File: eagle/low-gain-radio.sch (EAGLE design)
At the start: 124 parts, among them U1 MKW01Z128, U2 SKY65116, U3 W25Q80DV, U4 LP5907MFX-3.3, U5 NC7SZ05, U6 LP5907MFX-3.3, U7 LD39200, U8 MAAL-010704, U9 SKY13405-490LF, Y1 32MHz

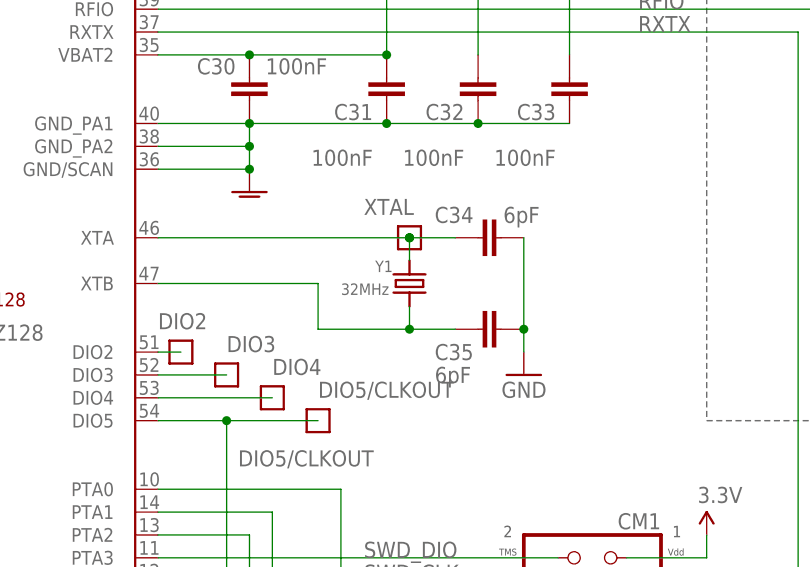
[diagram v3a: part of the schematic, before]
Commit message: Changed crystal symbol to get gnd working on the layout
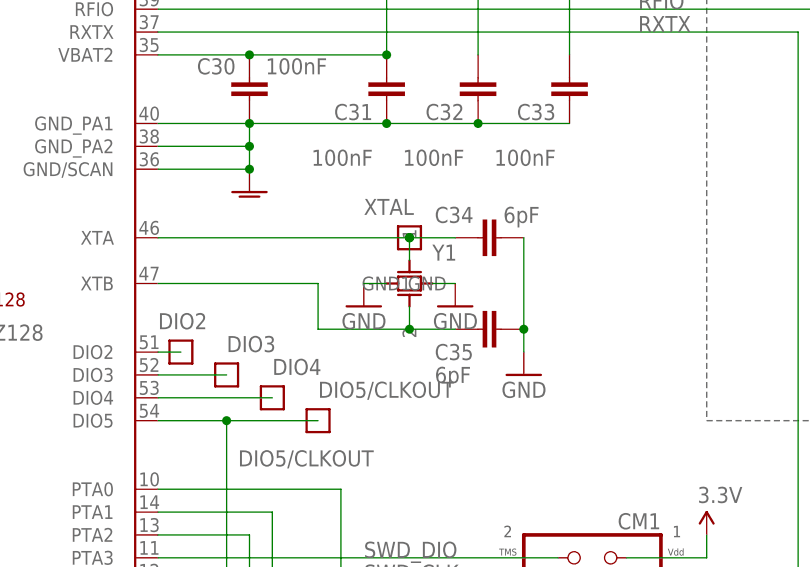
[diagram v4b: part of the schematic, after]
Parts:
- Y1: value 32MHz -> (none); device microbuilder:CRYSTAL2.5X2.0MM -> low-gain-radio:CRYSTAL2.5X2.0MM; DIST Digi-Key -> (none); DPN SER4044CT-ND -> (none); MFN EPSON -> (none); MPN FA20H 32.0000MF12Y-W3 -> (none)
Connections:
- net GND: now also Y1.GND, Y1.GND1
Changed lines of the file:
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@@
 <attribute name="MFG_PN" value="06035C104JAT2A"/>
-</part>
-<part name="Y1" library="microbuilder" deviceset="CRYSTAL" device="2.5X2.0MM" value="32MHz">
-<attribute name="DIST" value="Digi-Key"/>
-<attribute name="DPN" value="SER4044CT-ND"/>
-<attribute name="MFN" value="EPSON"/>
-<attribute name="MPN" value="FA20H 32.0000MF12Y-W3"/>
 </part>
 <part name="C34" library="rcl_custom" deviceset="C-EU" device="0603-B-NOSILK" value="6pF">
@@
 </part>
 <part name="GND15" library="psas_c3_team05" deviceset="GND" device=""/>
+<part name="Y1" library="low-gain-radio" deviceset="CRYSTAL" device="2.5X2.0MM"/>
+<part name="GND16" library="psas_c3_team05" deviceset="GND" device=""/>
+<part name="GND17" library="psas_c3_team05" deviceset="GND" device=""/>
 </parts>
 <sheets>
@@
 <attribute name="MFG_PN" x="180.34" y="218.44" size="1.778" layer="96" rot="R180" display="off"/>
 </instance>
-<instance part="Y1" gate="G$1" x="162.56" y="198.12" smashed="yes" rot="MR270">
-<attribute name="DIST" x="162.56" y="198.12" size="1.778" layer="96" rot="MR270" display="off"/>
-<attribute name="DPN" x="162.56" y="198.12" size="1.778" layer="96" rot="MR270" display="off"/>
-<attribute name="MFN" x="162.56" y="198.12" size="1.778" layer="96" rot="MR270" display="off"/>
-<attribute name="MPN" x="162.56" y="198.12" size="1.778" layer="96" rot="MR270" display="off"/>
-<attribute name="NAME" x="158.75" y="200.66" size="1.27" layer="95" rot="MR180"/>
-<attribute name="VALUE" x="154.94" y="198.12" size="1.27" layer="96" rot="MR180"/>
-</instance>
 <instance part="C34" gate="CE" x="172.72" y="203.2" smashed="yes" rot="MR90">
 <attribute name="NAME" x="165.354" y="206.629" size="1.778" layer="95" rot="MR180"/>
@@
 </instance>
 <instance part="GND15" gate="1" x="109.22" y="63.5"/>
+<instance part="Y1" gate="Y1" x="162.56" y="198.12"/>
+<instance part="GND16" gate="1" x="167.64" y="195.58" rot="MR0"/>
+<instance part="GND17" gate="1" x="157.48" y="195.58" rot="MR0"/>
 </instances>
 <busses>
@@
 <wire x1="109.22" y1="66.04" x2="109.22" y2="68.58" width="0.1524" layer="91"/>
 </segment>
+<segment>
+<pinref part="Y1" gate="Y1" pin="GND"/>
+<pinref part="GND17" gate="1" pin="GND"/>
+<wire x1="160.02" y1="198.12" x2="157.48" y2="198.12" width="0.1524" layer="91"/>
+</segment>
+<segment>
+<pinref part="Y1" gate="Y1" pin="GND1"/>
+<pinref part="GND16" gate="1" pin="GND"/>
+<wire x1="165.1" y1="198.12" x2="167.64" y2="198.12" width="0.1524" layer="91"/>
+</segment>
 </net>
 <net name="SWD_DIO" class="0">
@@
 <wire x1="134.62" y1="203.2" x2="162.56" y2="203.2" width="0.1524" layer="91"/>
 <pinref part="C34" gate="CE" pin="2"/>
-<pinref part="Y1" gate="G$1" pin="1"/>
 <wire x1="162.56" y1="203.2" x2="167.64" y2="203.2" width="0.1524" layer="91"/>
 <wire x1="162.56" y1="200.66" x2="162.56" y2="203.2" width="0.1524" layer="91"/>
@@
 <pinref part="XTAL" gate="G$1" pin="1"/>
 <junction x="162.56" y="203.2"/>
+<pinref part="Y1" gate="Y1" pin="1"/>
 </segment>
 </net>
@@
 <wire x1="152.4" y1="198.12" x2="134.62" y2="198.12" width="0.1524" layer="91"/>
 <pinref part="C35" gate="CE" pin="2"/>
-<pinref part="Y1" gate="G$1" pin="2"/>
 <wire x1="162.56" y1="195.58" x2="162.56" y2="193.04" width="0.1524" layer="91"/>
 <junction x="162.56" y="193.04"/>
-</segment>
-</net>
+<pinref part="Y1" gate="Y1" pin="2"/>
+</segment>
+</net>

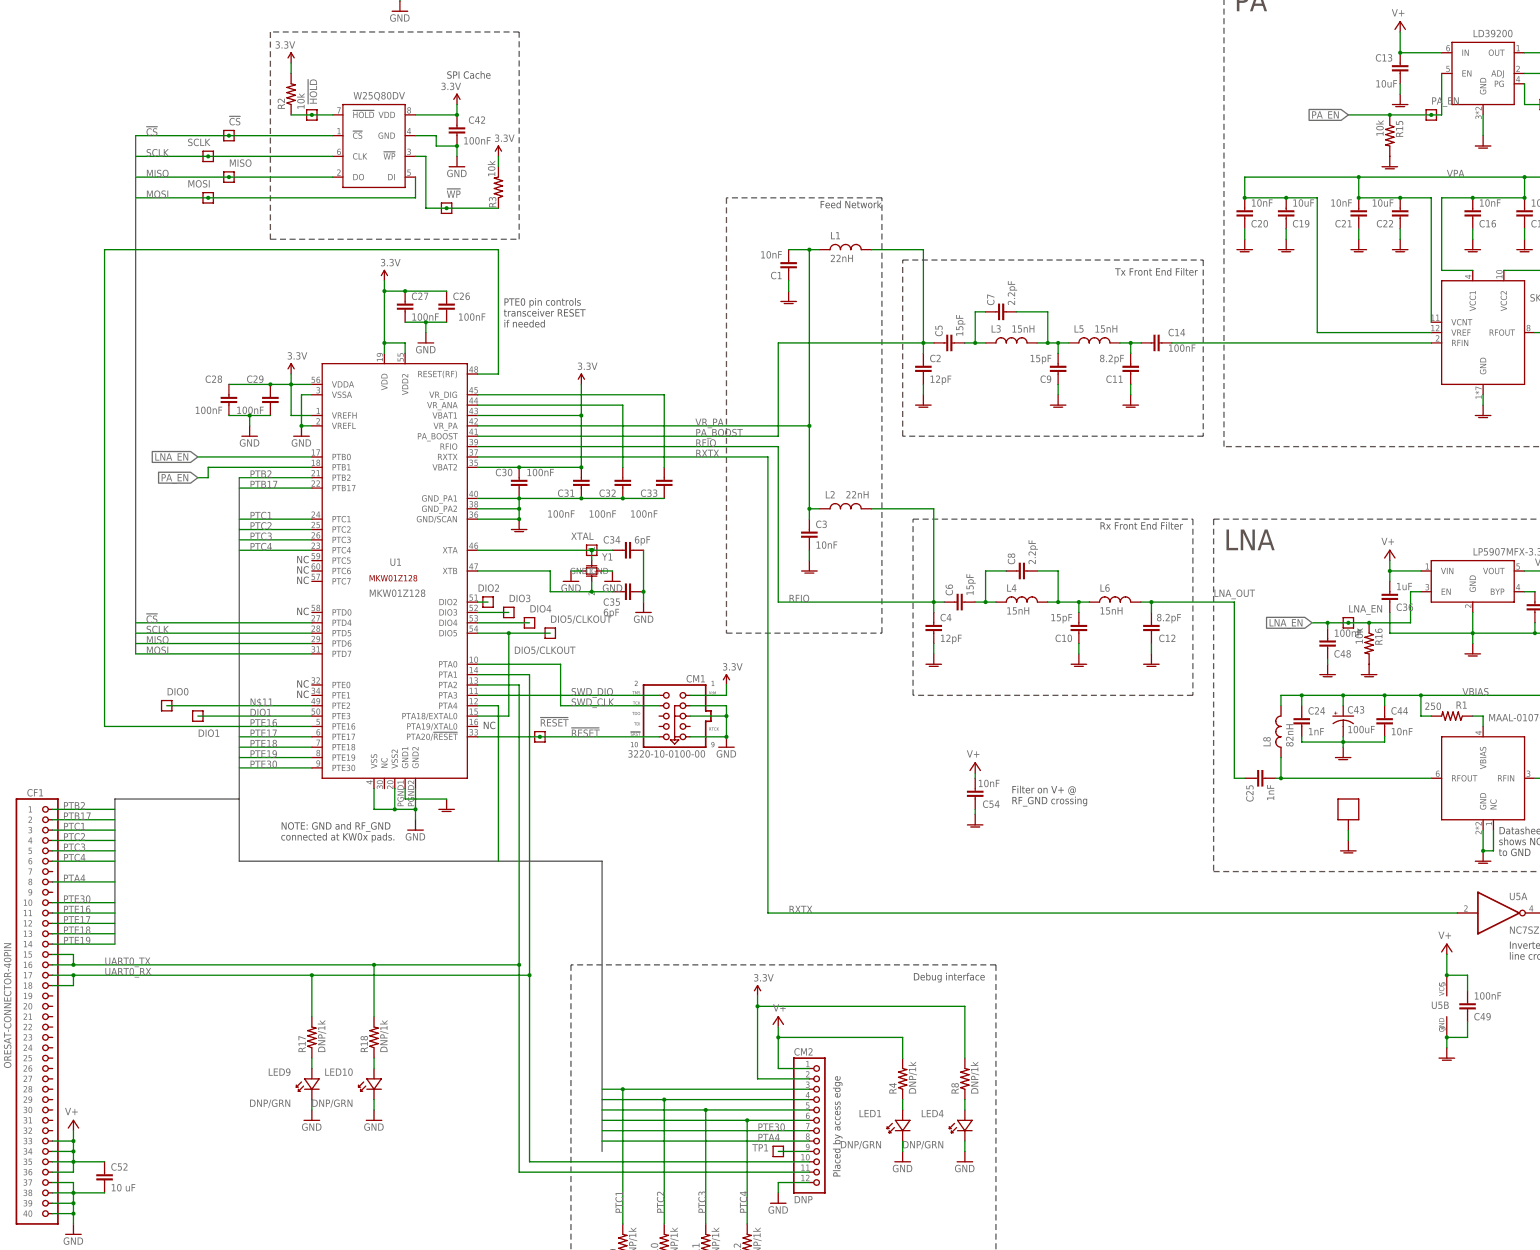
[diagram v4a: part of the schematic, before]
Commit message: Updated firmware
New: CMSIS submodule

Updated drivers
Added interrupt functionality
printf on uart0 with interrupts
doxygen template added
new project organization and test project
updated organization for firmware
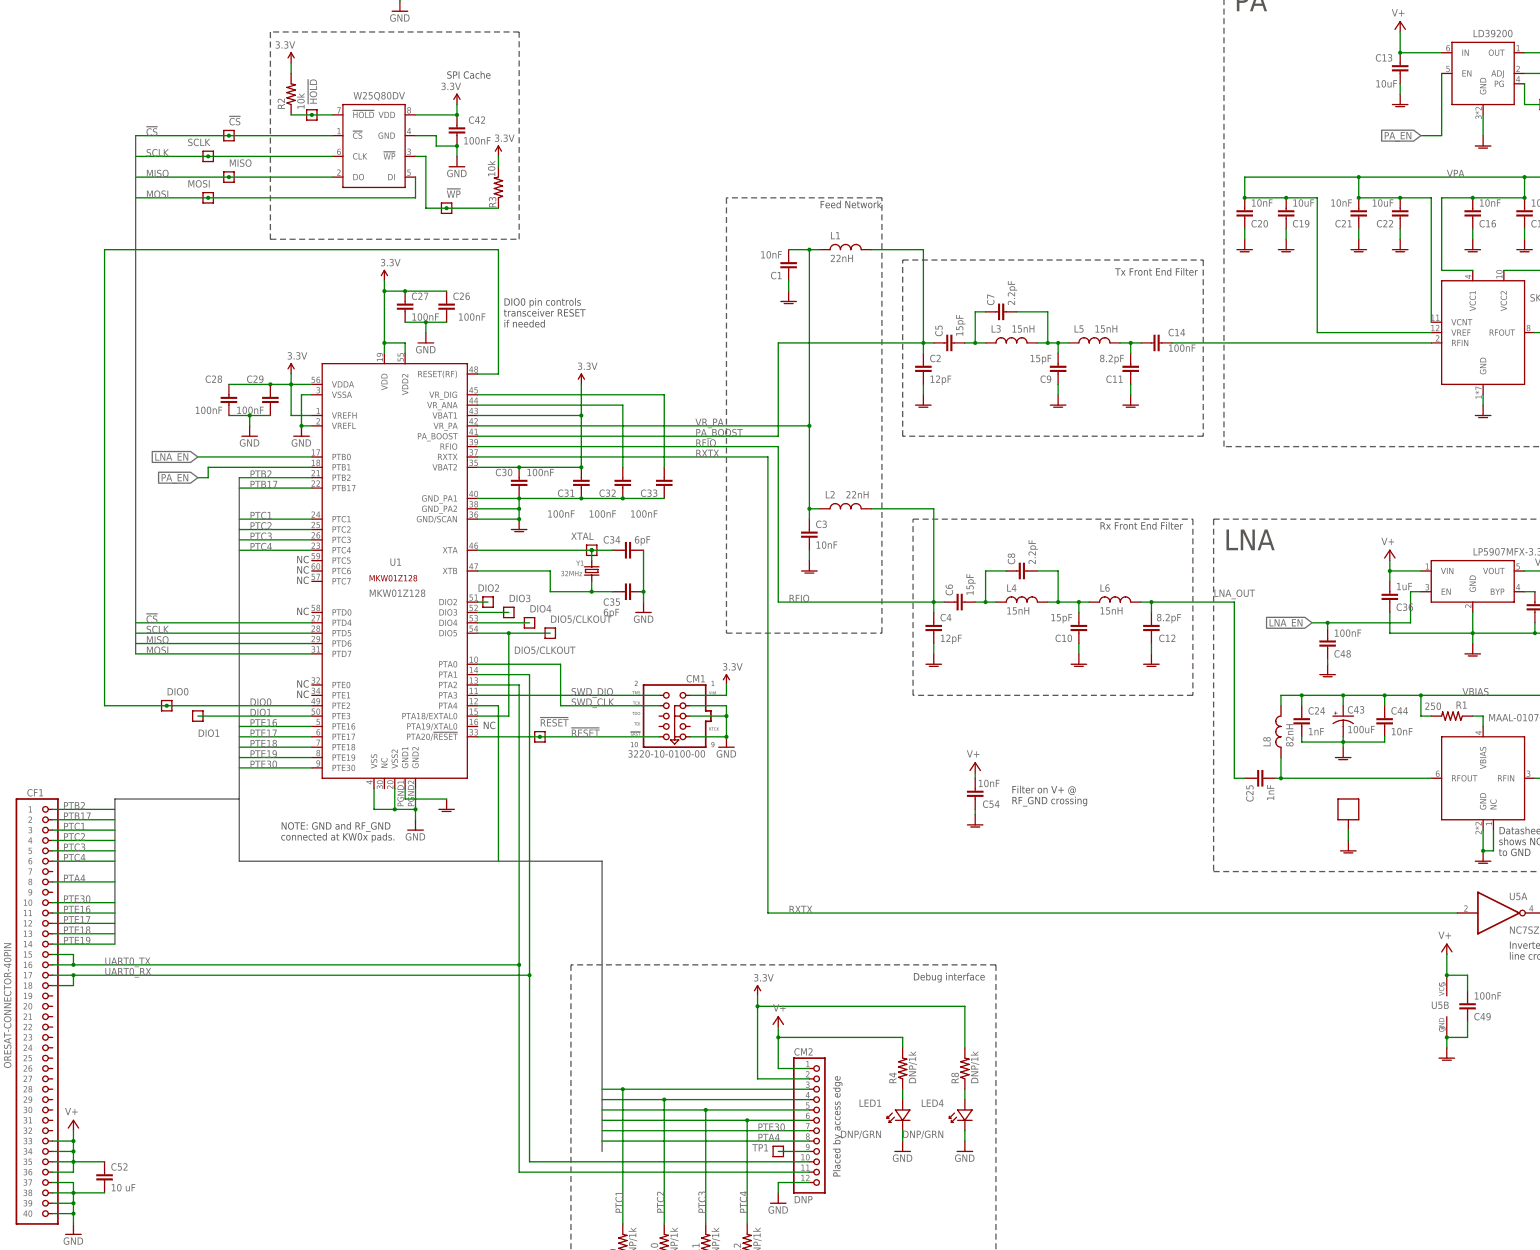
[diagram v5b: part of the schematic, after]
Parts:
- removed LED10, LED9: DNP/GRN, psas_c3_team05:LED-0603
- removed LNA_EN, PA_EN: TEST-POINT, Tova:TEST-POINT
- removed R15, R16: 10k, rcl_custom:R-US_0603-B-NOSILK
- removed R17, R18: DNP/1k, rcl_custom:R-US_0603-B-NOSILK
- Y1: value (none) -> 32MHz; device low-gain-radio:CRYSTAL2.5X2.0MM -> microbuilder:CRYSTAL2.5X2.0MM; DIST (none) -> Digi-Key; DPN (none) -> SER4044CT-ND; MFN (none) -> EPSON; MPN (none) -> FA20H 32.0000MF12Y-W3
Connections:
- removed net N$11: DIO0.1, U1.PTE2
- removed net N$6: LED9.A, R17.1
- removed net N$9: LED10.A, R18.1
- new net DIO0: DIO0.1, U1.PTE2, U1.RESET(RF)
- net GND: no longer LED10.K, LED9.K, Y1.GND, Y1.GND1
- net LNA_EN: no longer LNA_EN.1, R16.1
- net PA_EN: no longer PA_EN.1, R15.1
- net PTE16: no longer U1.RESET(RF)
- net RF_GND: no longer R15.2, R16.2
- net UART0_RX: no longer R17.2
- net UART0_TX: no longer R18.2
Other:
- note added: "DIO0 pin controls transceiver RESET if needed"
- note removed: "PTE0 pin controls transceiver RESET if needed"
- moved on the sheet: LED1, LED4, R4, R8

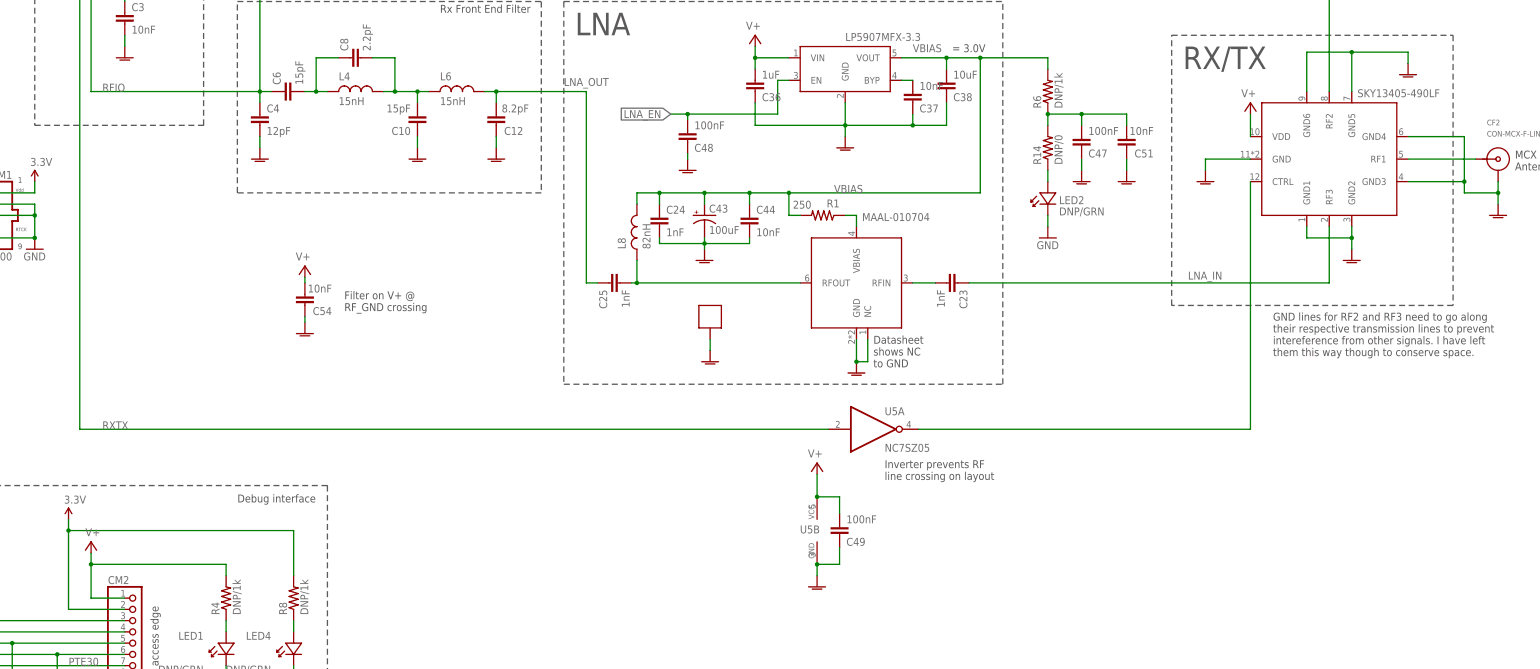
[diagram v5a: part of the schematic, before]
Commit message: Added new RF switch
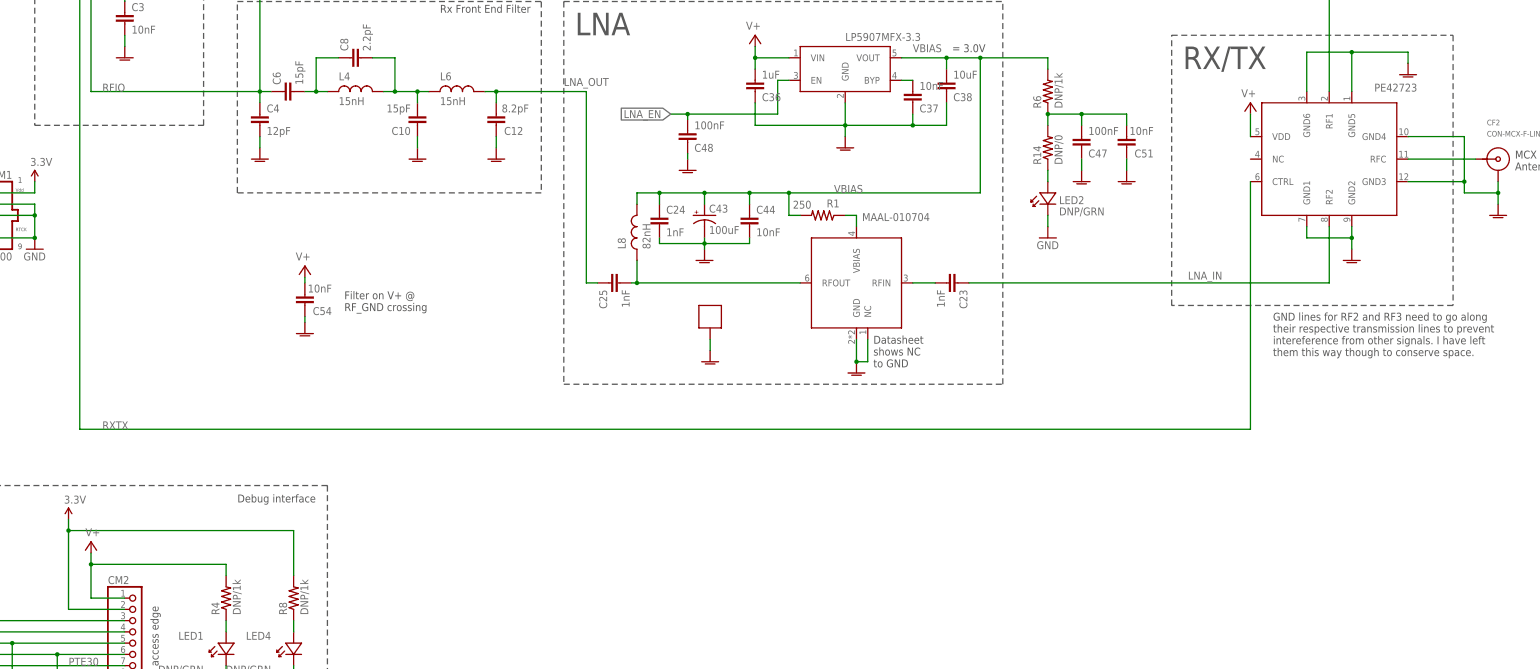
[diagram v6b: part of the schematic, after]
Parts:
- removed C49: 100nF, rcl_custom:C-EU0603-B-NOSILK
- removed U5: NC7SZ05, psas_c3_team05:NC7SZ05
- removed U9: SKY13405-490LF, psas_c3_team05:SKY13405-490LF
- added U$9: PE42723, low-gain-radio:PE42723
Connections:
- removed net !RXTX: U5A.OUT, U9.CTRL
- net LNA_IN: now also U$9.RF2; no longer U9.RF3
- net N$30: now also U$9.RFC; no longer U9.RF1
- net PA_IN: now also U$9.RF1; no longer U9.RF2
- net RF_GND: now also U$9.GND1, U$9.GND2, U$9.GND3, U$9.GND4, U$9.GND5, U$9.GND6; no longer C49.1, U5B.GND, U9.GND, U9.GND1, U9.GND2, U9.GND3, U9.GND4, U9.GND5, U9.GND6
- net RXTX: now also U$9.CTRL; no longer U5A.IN
- net V+: now also U$9.VDD; no longer C49.2, U5B.VCC, U9.VDD
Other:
- note removed: "Inverter prevents RF line crossing on layout"

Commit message: LGR SCHEMATIC AND BOARD REVISIONS
1. Added 0 ohms on VOUT of all LDOs
2. Created reflectometer circuit
3. Got rid of GPIO bus to 40 pin connector
4. Started layout for the 0ohm resistors and reflectometer but it got awfully messy and there are major changes that are going to be made to the board outline and antenna connector so I left them undone
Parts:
- removed CF2: CON-MCX-F-LINX-CONMCX003.062, oresat-eagle:CON-MCX-F-LINX-CONMCX003.062
- added C49, C55, C56, C57: 47nF, low-gain-radio:C-EU0402-C-NOSILK
- added D1, D2: 1N5711WS, microbuilder:DIODESOD-323
- added R15, R16, R17: 0, low-gain-radio:R-US_0805-C-NOSILK
- added R18, R19: 51, low-gain-radio:R-US_0402-C-NOSILK
- added R20, R21: 20k, low-gain-radio:R-US_0402-C-NOSILK
- added U$22: BDCN-20-13+, low-gain-radio:BDCN-20-13+
- CM1: device psas_c3_team05:JTAG_ARM-10-50MIL -> low-gain-radio:JTAG_ARM-10-50MIL
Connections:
- removed net N$30: CF2.CENTER, U$9.RFC
- removed net PTB17: CF1.2, U1.PTB17
- removed net PTB2: CF1.1, U1.PTB2
- removed net PTE16: CF1.11, U1.PTE16
- removed net PTE17: CF1.12, U1.PTE17
- removed net PTE18: CF1.13, U1.PTE18
- removed net PTE19: CF1.14, U1.PTE19
- new net DC_OUT: U$22.OUT
- new net FWD: D2.A, R19.2, U$22.FWD
- new net N$11: R17.1, U6.VOUT
- new net N$24: C49.1, D1.C, R20.2
- new net N$28: C57.1, D2.C, R21.2
- new net N$6: C41.2, C53.1, R15.1, U4.VOUT
- new net N$9: R16.1, U7.OUT
- new net REV: D1.A, R18.2, U$22.REV
- new net RFC: U$22.IN, U$9.RFC
- new net RF_RESET: U1.PTE16, U1.RESET(RF)
- new net VFWD: C56.1, R21.1, U1.PTE17
- new net VREV: C55.1, R20.1, U1.PTE18
- net 3.3V: now also R15.2; no longer C41.2, C53.1, U4.VOUT
- net DIO0: no longer U1.RESET(RF)
- net PTA4: no longer CF1.8
- net PTC1: no longer CF1.3
- net PTC2: no longer CF1.4
- net PTC3: no longer CF1.5
- net PTC4: no longer CF1.6
- net PTE30: no longer CF1.10
- net RF_GND: now also C49.2, C55.2, C56.2, C57.2, R18.1, R19.1, U$22.GND, U$22.GND2; no longer CF2.SHIELD
- net VBIAS: now also R17.2; no longer U6.VOUT
- net VPA: now also R16.2; no longer U7.OUT
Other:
- note added: "Reflectometer"
- moved on the sheet: C38, C46, DIO0
